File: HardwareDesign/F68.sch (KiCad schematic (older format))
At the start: 0 parts

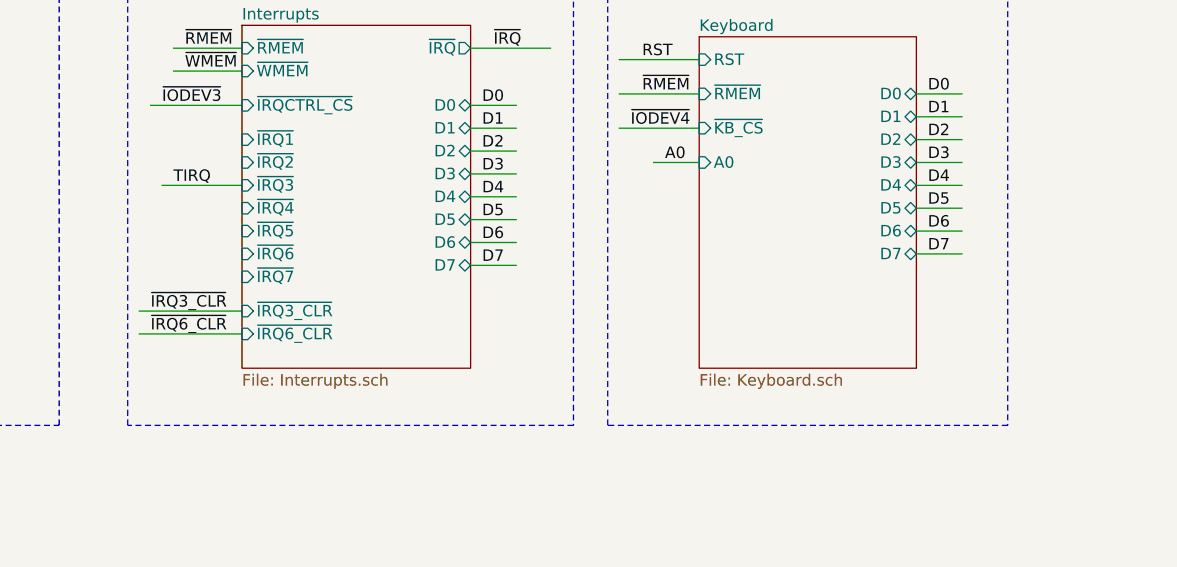
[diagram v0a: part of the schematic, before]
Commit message: more preparations for PCB layout
More nets connected to appropriate backplane connector pin.
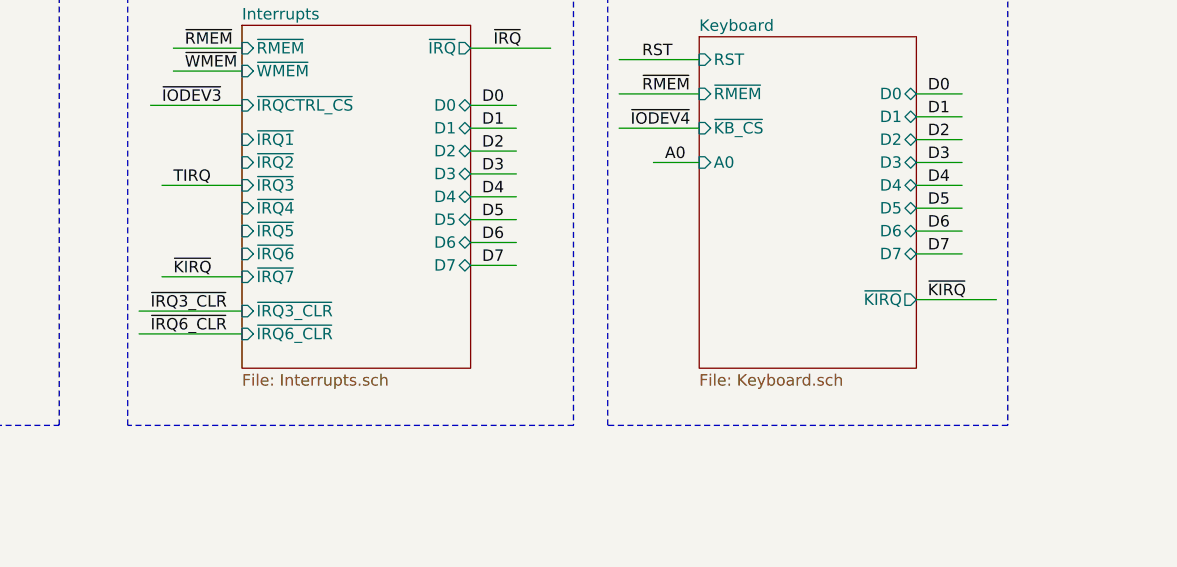
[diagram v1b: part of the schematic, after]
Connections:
- net labels added: ~KIRQ~
- wire segments 111 -> 113
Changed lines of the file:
@@
 F12 "D7" B R 7750 6350 50
 F13 "RST" I L 6800 5500 50
+F14 "~KIRQ~" O R 7750 6550 50
 $EndSheet
 Wire Wire Line
@@
 Text Label 6650 5950 0    50   ~ 0
 A0
+Wire Wire Line
+	7750 6550 8100 6550
+Text Label 7800 6550 0    50   ~ 0
+~KIRQ~
+Wire Wire Line
+	4450 6450 4800 6450
+Text Label 4500 6450 0    50   ~ 0
+~KIRQ~
 $EndSCHEMATC

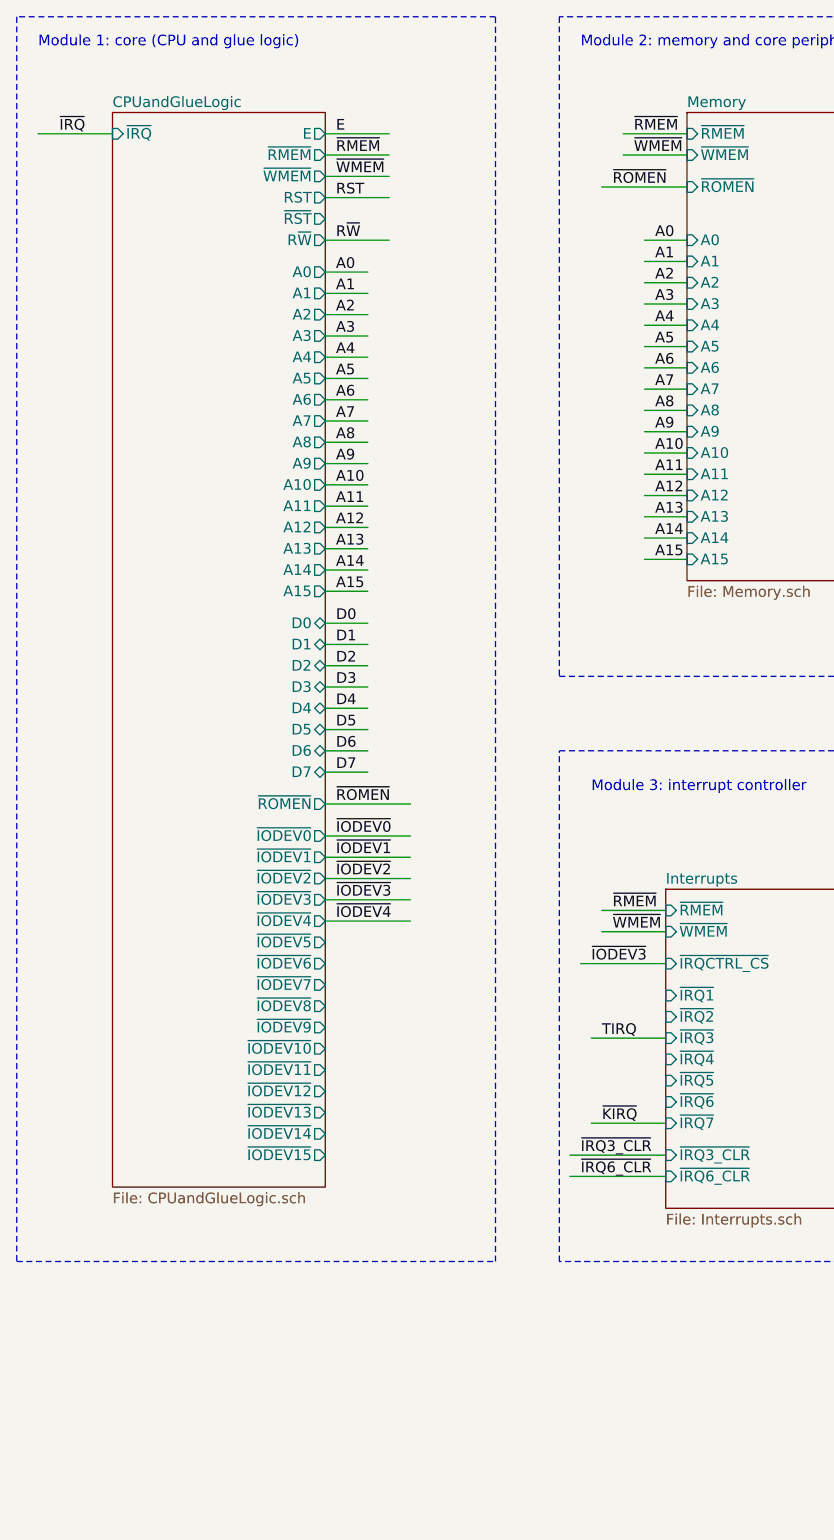
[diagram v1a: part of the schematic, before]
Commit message: more preparations for PCB layout
Make sure all nets connected to backplane connector pins are
labeled correctly.

Add bulk decoupling caps for each backplane connector.

Make keyboard interrupt be -IRQ5 rather than -IRQ7.
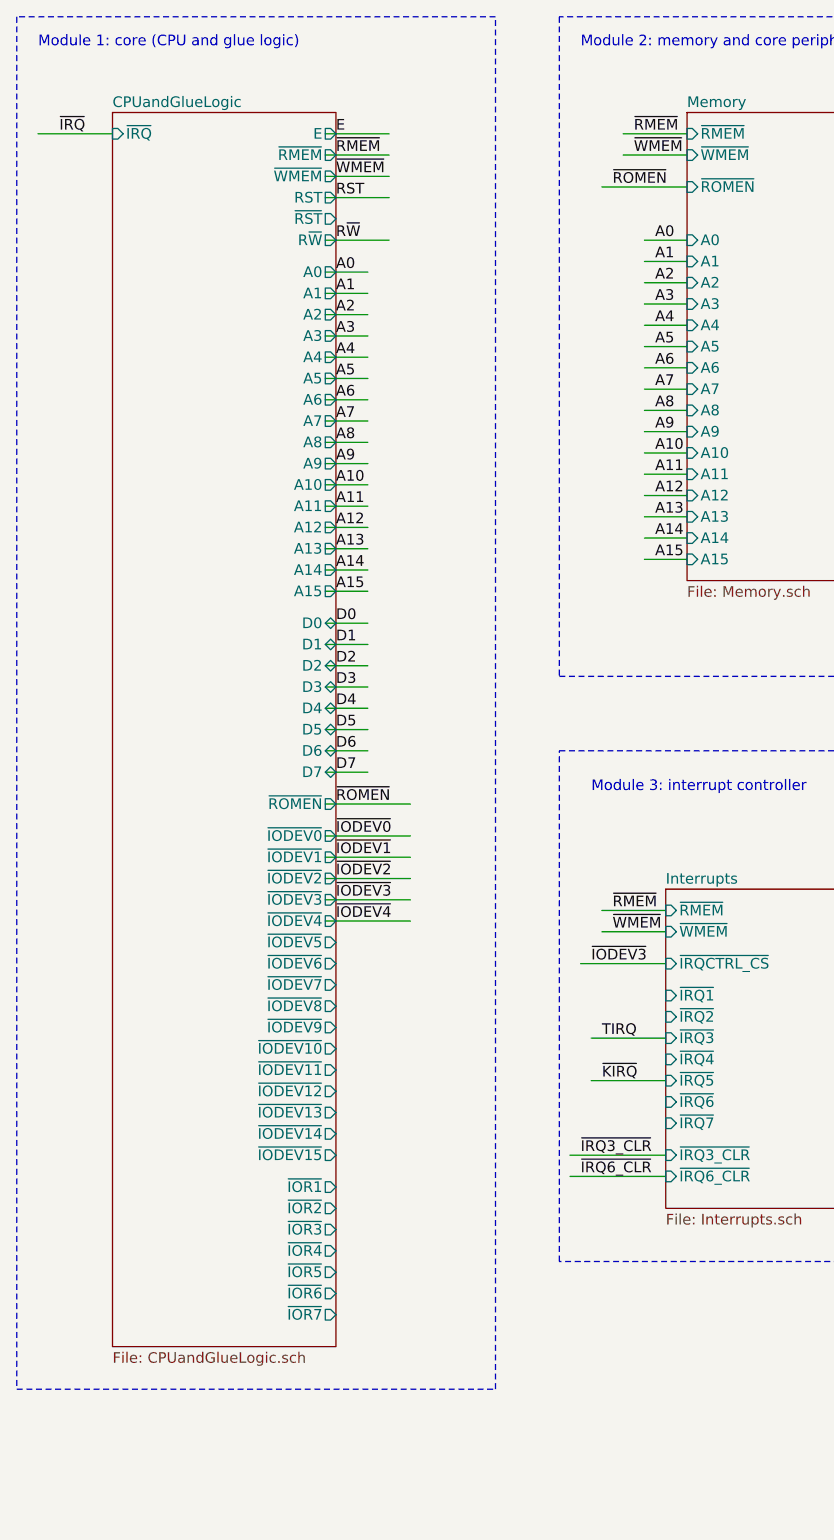
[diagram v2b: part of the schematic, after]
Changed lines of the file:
@@
 F68: A DIY 6809 microcomputer system
 $Sheet
-S 2200 1700 1000 5050
+S 2200 1700 1050 5800
 U 5CFA6AAA
 F0 "CPUandGlueLogic" 50
 F1 "CPUandGlueLogic.sch" 50
-F2 "A0" O R 3200 2450 50
-F3 "A1" O R 3200 2550 50
-F4 "A2" O R 3200 2650 50
-F5 "A3" O R 3200 2750 50
-F6 "A4" O R 3200 2850 50
-F7 "A5" O R 3200 2950 50
-F8 "A6" O R 3200 3050 50
-F9 "A7" O R 3200 3150 50
-F10 "A8" O R 3200 3250 50
-F11 "A9" O R 3200 3350 50
-F12 "A10" O R 3200 3450 50
-F13 "A11" O R 3200 3550 50
-F14 "A12" O R 3200 3650 50
-F15 "A13" O R 3200 3750 50
-F16 "A14" O R 3200 3850 50
-F17 "A15" O R 3200 3950 50
-F18 "D0" B R 3200 4100 50
-F19 "D1" B R 3200 4200 50
-F20 "D2" B R 3200 4300 50
-F21 "D3" B R 3200 4400 50
-F22 "D4" B R 3200 4500 50
-F23 "D5" B R 3200 4600 50
-F24 "D6" B R 3200 4700 50
-F25 "D7" B R 3200 4800 50
-F26 "E" O R 3200 1800 50
-F27 "~RMEM~" O R 3200 1900 50
-F28 "~WMEM~" O R 3200 2000 50
-F29 "RST" O R 3200 2100 50
-F30 "~RST~" O R 3200 2200 50
-F31 "~IODEV0~" O R 3200 5100 50
-F32 "~IODEV1~" O R 3200 5200 50
-F33 "~IODEV2~" O R 3200 5300 50
-F34 "~IODEV3~" O R 3200 5400 50
-F35 "~IODEV4~" O R 3200 5500 50
-F36 "~IODEV5~" O R 3200 5600 50
-F37 "~IODEV6~" O R 3200 5700 50
-F38 "~IODEV7~" O R 3200 5800 50
-F39 "~IODEV8~" O R 3200 5900 50
-F40 "~IODEV9~" O R 3200 6000 50
-F41 "~IODEV10~" O R 3200 6100 50
-F42 "~IODEV11~" O R 3200 6200 50
-F43 "~IODEV12~" O R 3200 6300 50
-F44 "~IODEV13~" O R 3200 6400 50
-F45 "~IODEV14~" O R 3200 6500 50
-F46 "~IODEV15~" O R 3200 6600 50
-F47 "~ROMEN~" O R 3200 4950 50
-F48 "R~W" O R 3200 2300 50
+F2 "A0" O R 3250 2450 50
+F3 "A1" O R 3250 2550 50
+F4 "A2" O R 3250 2650 50
+F5 "A3" O R 3250 2750 50
+F6 "A4" O R 3250 2850 50
+F7 "A5" O R 3250 2950 50
+F8 "A6" O R 3250 3050 50
+F9 "A7" O R 3250 3150 50
+F10 "A8" O R 3250 3250 50
+F11 "A9" O R 3250 3350 50
+F12 "A10" O R 3250 3450 50
+F13 "A11" O R 3250 3550 50
+F14 "A12" O R 3250 3650 50
+F15 "A13" O R 3250 3750 50
+F16 "A14" O R 3250 3850 50
+F17 "A15" O R 3250 3950 50
+F18 "D0" B R 3250 4100 50
+F19 "D1" B R 3250 4200 50
+F20 "D2" B R 3250 4300 50
+F21 "D3" B R 3250 4400 50
+F22 "D4" B R 3250 4500 50
+F23 "D5" B R 3250 4600 50
+F24 "D6" B R 3250 4700 50
+F25 "D7" B R 3250 4800 50
+F26 "E" O R 3250 1800 50
+F27 "~RMEM~" O R 3250 1900 50
+F28 "~WMEM~" O R 3250 2000 50
+F29 "RST" O R 3250 2100 50
+F30 "~RST~" O R 3250 2200 50
+F31 "~IODEV0~" O R 3250 5100 50
+F32 "~IODEV1~" O R 3250 5200 50
+F33 "~IODEV2~" O R 3250 5300 50
+F34 "~IODEV3~" O R 3250 5400 50
+F35 "~IODEV4~" O R 3250 5500 50
+F36 "~IODEV5~" O R 3250 5600 50
+F37 "~IODEV6~" O R 3250 5700 50
+F38 "~IODEV7~" O R 3250 5800 50
+F39 "~IODEV8~" O R 3250 5900 50
+F40 "~IODEV9~" O R 3250 6000 50
+F41 "~IODEV10~" O R 3250 6100 50
+F42 "~IODEV11~" O R 3250 6200 50
+F43 "~IODEV12~" O R 3250 6300 50
+F44 "~IODEV13~" O R 3250 6400 50
+F45 "~IODEV14~" O R 3250 6500 50
+F46 "~IODEV15~" O R 3250 6600 50
+F47 "~ROMEN~" O R 3250 4950 50
+F48 "R~W" O R 3250 2300 50
 F49 "~IRQ" I L 2200 1800 50
+F50 "~IOR1~" O R 3250 6750 50
+F51 "~IOR2~" O R 3250 6850 50
+F52 "~IOR3~" O R 3250 6950 50
+F53 "~IOR4~" O R 3250 7050 50
+F54 "~IOR5~" O R 3250 7150 50
+F55 "~IOR6~" O R 3250 7250 50
+F56 "~IOR7~" O R 3250 7350 50
 $EndSheet
 $Sheet
@@
 ~IODEV2
 Wire Notes Line
-	1750 1250 1750 7100
-Wire Notes Line
-	1750 7100 4000 7100
-Wire Notes Line
-	4000 7100 4000 1250
+	1750 1250 1750 7700
+Wire Notes Line
+	1750 7700 4000 7700
+Wire Notes Line
+	4000 7700 4000 1250
 Wire Notes Line
 	4000 1250 1750 1250
@@
 ~KIRQ~
 Wire Wire Line
-	4450 6450 4800 6450
-Text Label 4500 6450 0    50   ~ 0
+	4450 6250 4800 6250
+Text Label 4500 6250 0    50   ~ 0
 ~KIRQ~
 $EndSCHEMATC

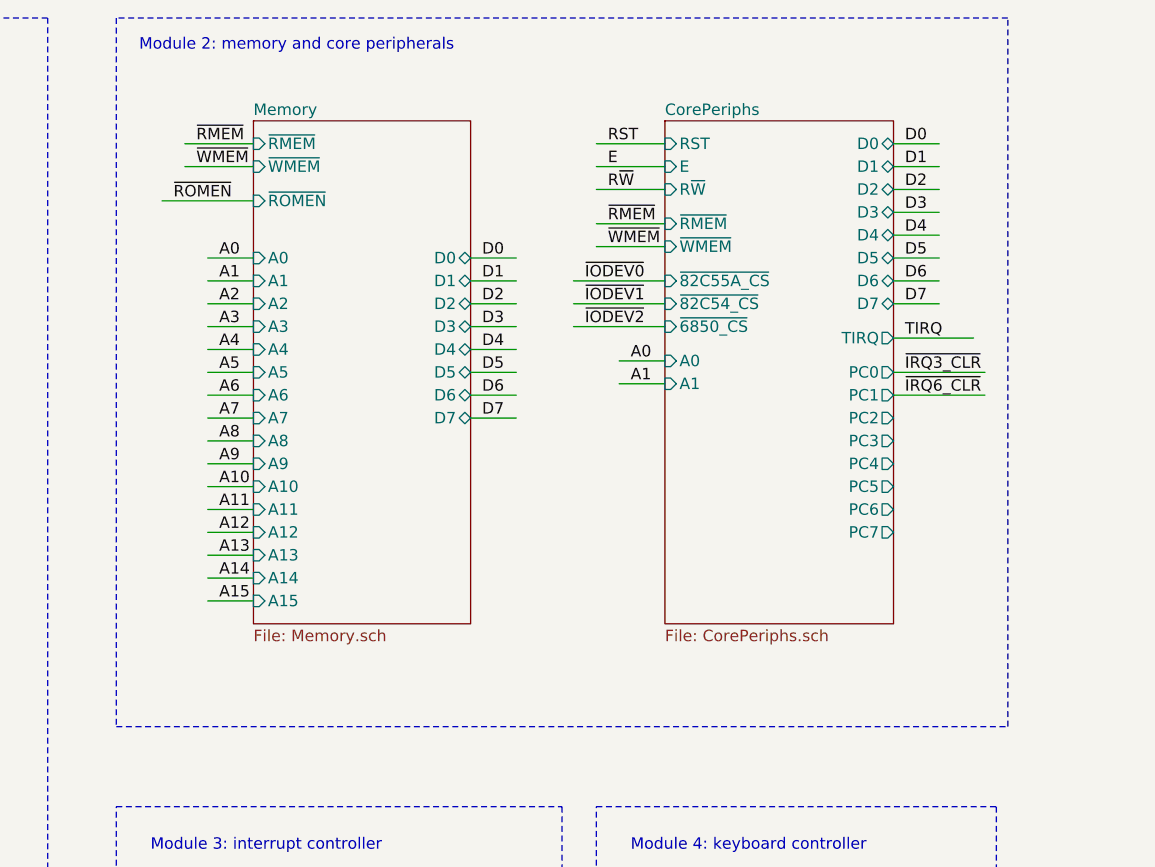
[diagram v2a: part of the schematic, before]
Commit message: a few more consistency tweaks before PCB layout
Routed second timer/counter output to backplane connector,
just in case we want to use it for something eventually
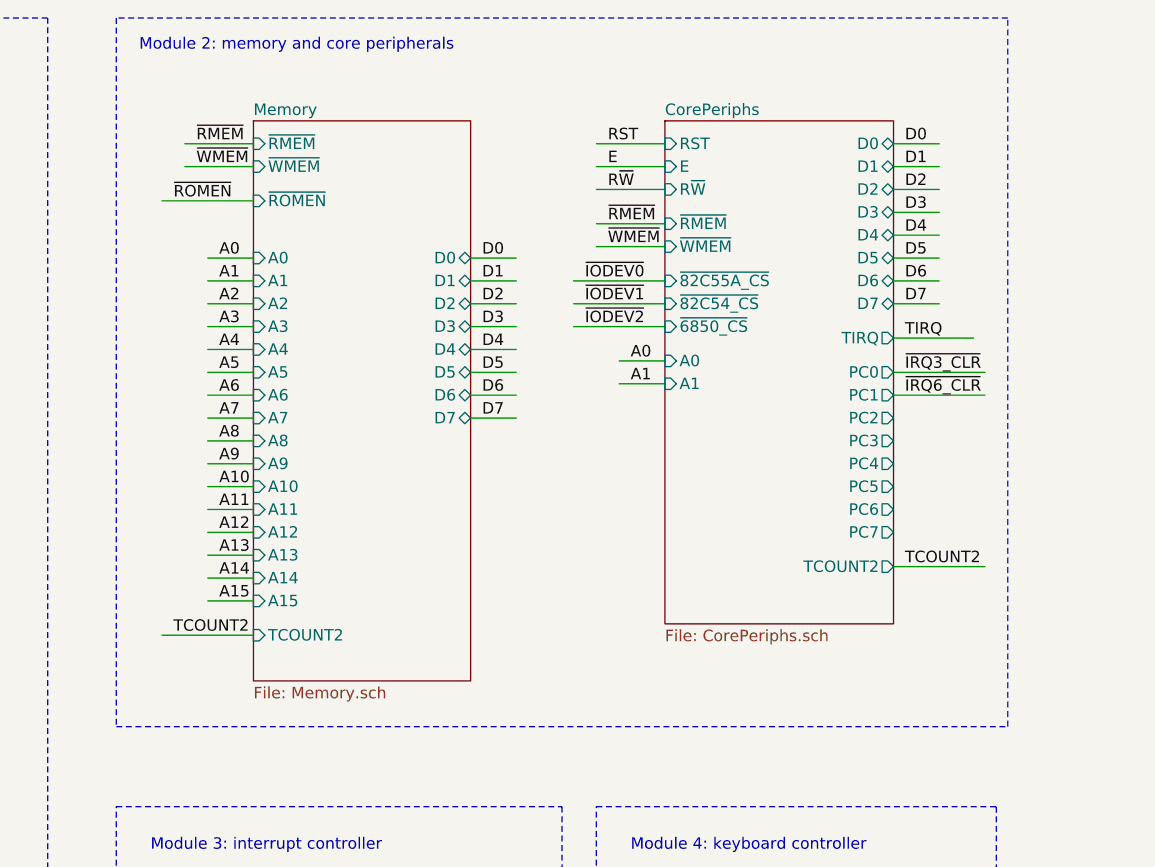
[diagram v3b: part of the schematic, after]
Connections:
- net labels added: TCOUNT2
- wire segments 113 -> 115
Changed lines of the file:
@@
 $EndSheet
 $Sheet
-S 4900 1700 950  2200
+S 4900 1700 950  2450
 U 5D49B078
 F0 "Memory" 50
@@
 F27 "D7" B R 5850 3000 50
 F28 "A15" I L 4900 3800 50
+F29 "TCOUNT2" I L 4900 3950 50
 $EndSheet
 Wire Wire Line
@@
 F27 "PC6" O R 7700 3400 50
 F28 "PC7" O R 7700 3500 50
+F29 "TCOUNT2" O R 7700 3650 50
 $EndSheet
 Wire Wire Line
@@
 Text Label 4500 6250 0    50   ~ 0
 ~KIRQ~
+Wire Wire Line
+	7700 3650 8100 3650
+Text Label 7750 3650 0    50   ~ 0
+TCOUNT2
+Wire Wire Line
+	4500 3950 4900 3950
+Text Label 4550 3950 0    50   ~ 0
+TCOUNT2
 $EndSCHEMATC
